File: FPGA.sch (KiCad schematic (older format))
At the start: 14 parts, among them U34 PCA9555AHF,128, U39 PCA9555AHF,128, U59 TCA9517DGKR

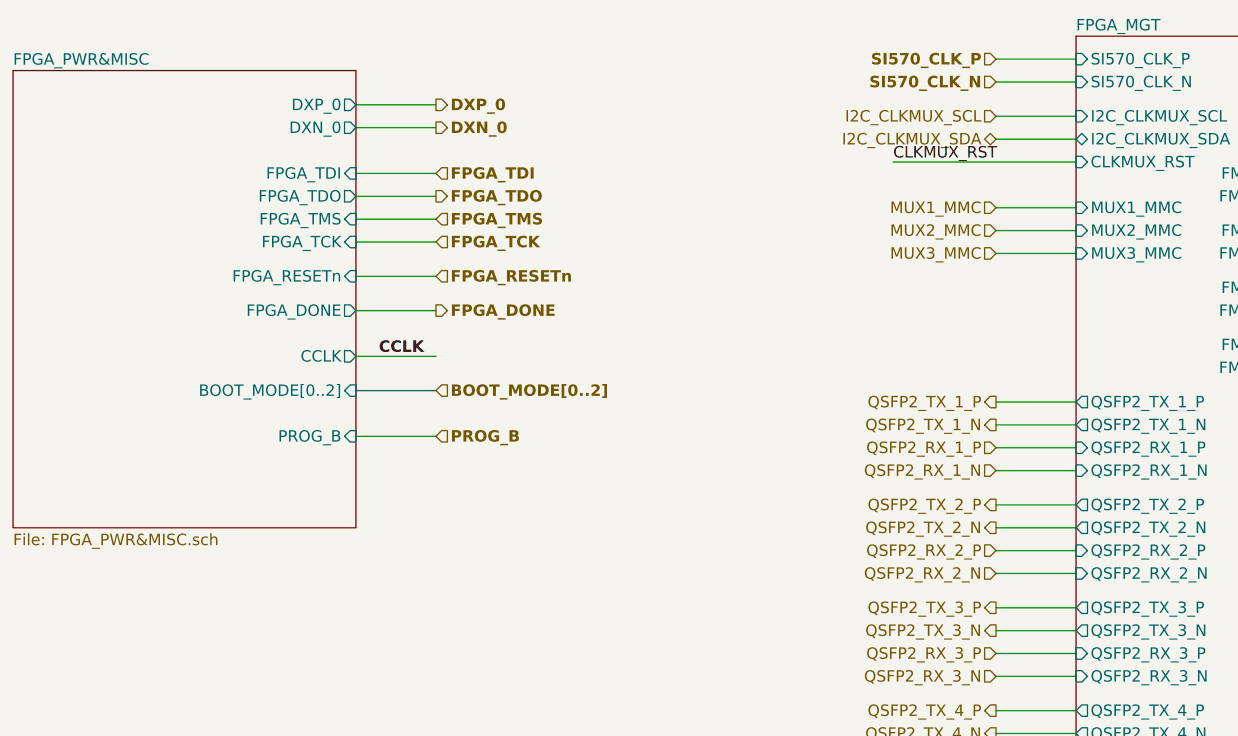
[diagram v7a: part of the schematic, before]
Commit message: fixed issue with FPGA booting by adding POWER GOOD signal to keep FPGA in reset during power on; U36 and U37 BIAS connected to 3V3P; added other transistor to reset clock mux during power on
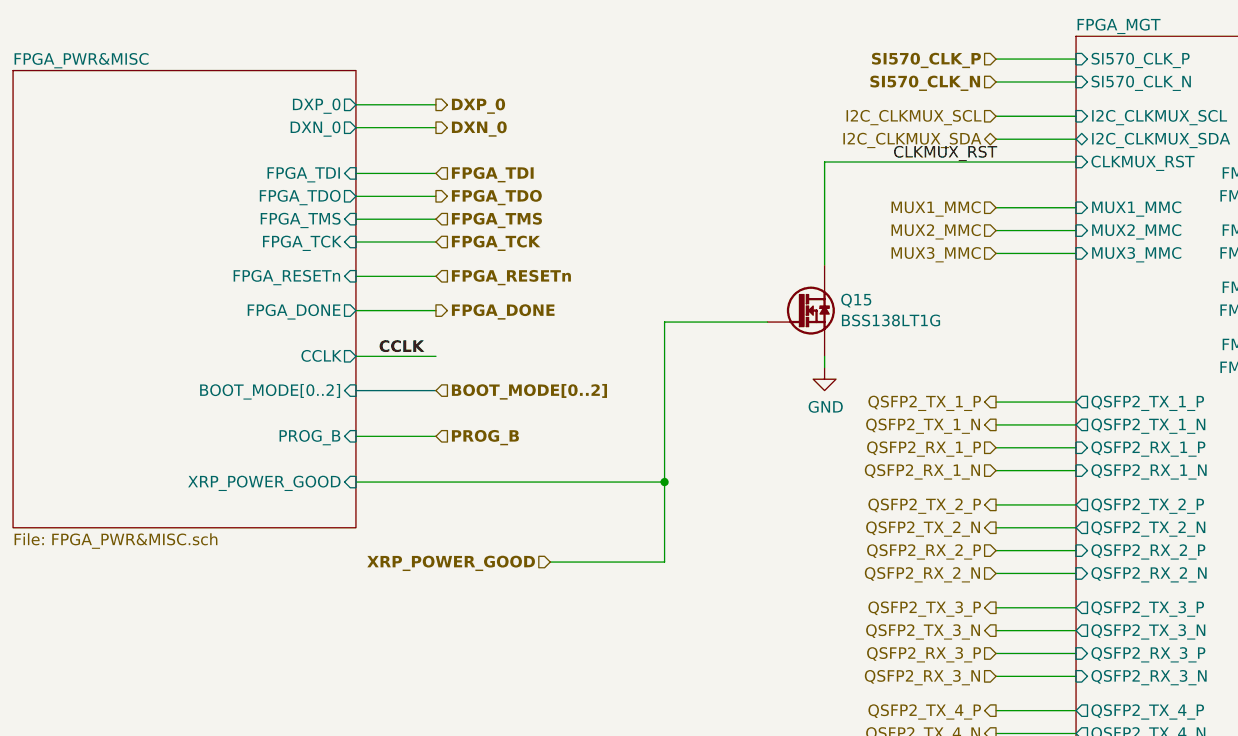
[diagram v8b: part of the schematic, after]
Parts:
- added Q15: BSS138LT1G, ICs And Semiconductors SMD:SOT95P240X110-3N, symbol Transistors:BSS138LT1G
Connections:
- net labels added: XRP_POWER_GOOD
- wire segments 187 -> 194
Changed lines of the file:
@@
 F11 "BOOT_MODE[0..2]" I R 3850 6450 50
 F12 "PROG_B" I R 3850 6650 50
+F13 "XRP_POWER_GOOD" I R 3850 6850 50
 $EndSheet
 Wire Wire Line
@@
 Text Label 6200 5450 0    50   ~ 0
 CLKMUX_RST
-Wire Wire Line
-	6200 5450 7000 5450
 Text Label 8500 9850 0    50   ~ 0
 CLKMUX_RST
@@
 Connection ~ 12900 8850
 Connection ~ 13000 7950
+Text HLabel 4700 7200 0    50   Input ~ 10
+XRP_POWER_GOOD
+$Comp
+L power:GND #PWR?
+U 1 1 60A21969
+P 5900 6350
+AR Path="/5BD32060/60A21969" Ref="#PWR?"  Part="1"
+AR Path="/5BABAC65/60A21969" Ref="#PWR?"  Part="1"
+AR Path="/5CC24E97/60A21969" Ref="#PWR?"  Part="1"
+AR Path="/5CC393D3/60A21969" Ref="#PWR?"  Part="1"
+AR Path="/5CC6DBF7/60A21969" Ref="#PWR?"  Part="1"
+AR Path="/5CC8AFE1/60A21969" Ref="#PWR?"  Part="1"
+AR Path="/5C907554/5C417BCB/60A21969" Ref="#PWR?"  Part="1"
+AR Path="/5C907554/60A21969" Ref="#PWR030"  Part="1"
+F 0 "#PWR030" H 5900 6100 50  0001 C CNN
+F 1 "GND" H 5905 6177 50  0000 C CNN
+F 2 "" H 5900 6350 50  0001 C CNN
+F 3 "" H 5900 6350 50  0001 C CNN
+	1    5900 6350
+	1    0    0    -1
+$EndComp
+Wire Wire Line
+	5900 6300 5900 6350
+$Comp
+L Transistors:BSS138LT1G Q?
+U 1 1 60A21990
+P 5650 6150
+AR Path="/5C907554/5C417BCB/60A21990" Ref="Q?"  Part="1"
+AR Path="/5C907554/60A21990" Ref="Q15"  Part="1"
+F 0 "Q15" H 5969 6246 50  0000 L CNN
+F 1 "BSS138LT1G" H 5969 6155 50  0000 L CNN
+F 2 "ICs And Semiconductors SMD:SOT95P240X110-3N" H 5650 4940 60  0001 L CNN
+F 3 "\\\\cern.ch\\dfs\\Applications\\Altium\\Datasheets\\BSS138LT1G.pdf" H 5650 5660 60  0001 L CNN
+F 4 "BSS138LT1G" H 5650 5570 60  0001 L CNN "Part Number"
+F 5 "N-MOSFET-D 1G 2S 3D" H 5650 5480 60  0001 L CNN "Library Ref"
+F 6 "SchLib\\Transistors.SchLib" H 5650 5390 60  0001 L CNN "Library Path"
+F 7 "BSS138LT1G" H 5650 5300 60  0001 L CNN "Comment"
+F 8 "Standard" H 5650 5210 60  0001 L CNN "Component Kind"
+F 9 "Standard" H 5650 5120 60  0001 L CNN "Component Type"
+F 10 "BSS138LT1G" H 5650 5030 60  0001 L CNN "Device"
+F 11 "SOT23 3-Leads, Pitch 0.95mm - Body 1.4x3mm, IPC Medium Density" H 5650 4850 60  0001 L CNN "PackageDescription"
+F 12 " " H 5650 4760 60  0001 L CNN "Status"
+F 13 "50V 200mA N-Channel Enhancement Mode Field-Effect Transistor" H 5650 4670 60  0001 L CNN "Part Description"
+F 14 "ON SEMICONDUCTOR" H 5650 4580 60  0001 L CNN "Manufacturer"
+F 15 "BSS138LT1G" H 5650 4490 60  0001 L CNN "Manufacturer Part Number"
+F 16 "3" H 5650 4400 60  0001 L CNN "Pin Count"
+F 17 "SOT23-3" H 5650 4310 60  0001 L CNN "Case"
+F 18 "Yes" H 5650 4220 60  0001 L CNN "Mounted"
+F 19 "No" H 5650 4130 60  0001 L CNN "Socket"
+F 20 "No" H 5650 4040 60  0001 L CNN "PressFit"
+F 21 "Yes" H 5650 3950 60  0001 L CNN "SMD"
+F 22 "No" H 5650 3860 60  0001 L CNN "Sense"
+F 23 " " H 5650 3770 60  0001 L CNN "Sense Comment"
+F 24 "No" H 5650 3680 60  0001 L CNN "Bonding"
+F 25 " " H 5650 3590 60  0001 L CNN "Status Comment"
+F 26 "1.11mm" H 5650 3500 60  0001 L CNN "ComponentHeight"
+F 27 "PcbLib\\ICs And Semiconductors SMD.PcbLib" H 5650 3410 60  0001 L CNN "Footprint Path"
+F 28 "SOT95P240X110-3N" H 5650 3320 60  0001 L CNN "Footprint Ref"
+F 29 " " H 5650 3050 60  0001 L CNN "ComponentLink1Description"
+F 30 " " H 5650 2870 60  0001 L CNN "ComponentLink2Description"
+F 31 "CERN DEM JLC" H 5650 2780 60  0001 L CNN "Author"
+F 32 "03/23/09 00:00:00" H 5650 2690 60  0001 L CNN "CreateDate"
+F 33 "03/23/09 00:00:00" H 5650 2600 60  0001 L CNN "LatestRevisionDate"
+F 34 "ICs And Semiconductors SMD" H 5650 2510 60  0001 L CNN "Library Name"
+F 35 "This work is licensed under the Creative Commons CC-BY-SA 4.0 License. To the extent that circuit schematics that use Licensed Material can be considered to be ‘Adapted Material’, then the copyright holder waives article 3.b of the license with respect to these schematics." H 5650 2420 60  0001 L CNN "License"
+	1    5650 6150
+	1    0    0    -1
+$EndComp
+Wire Wire Line
+	5900 5450 5900 5900
+Wire Wire Line
+	5900 5450 7000 5450
+Wire Wire Line
+	5650 6150 5200 6150
+Wire Wire Line
+	5200 6150 5200 6850
+Wire Wire Line
+	3850 6850 5200 6850
+Wire Wire Line
+	4700 7200 5200 7200
+Wire Wire Line
+	5200 7200 5200 6850
+Connection ~ 5200 6850
 $EndSCHEMATC
